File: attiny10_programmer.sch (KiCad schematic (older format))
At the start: 12 parts, among them J1 Conn_01x03, J2 AVR-ISP-6, Q1 Q_PNP_EBC, U1 SFH617A-1, U2 ATtiny10-TS

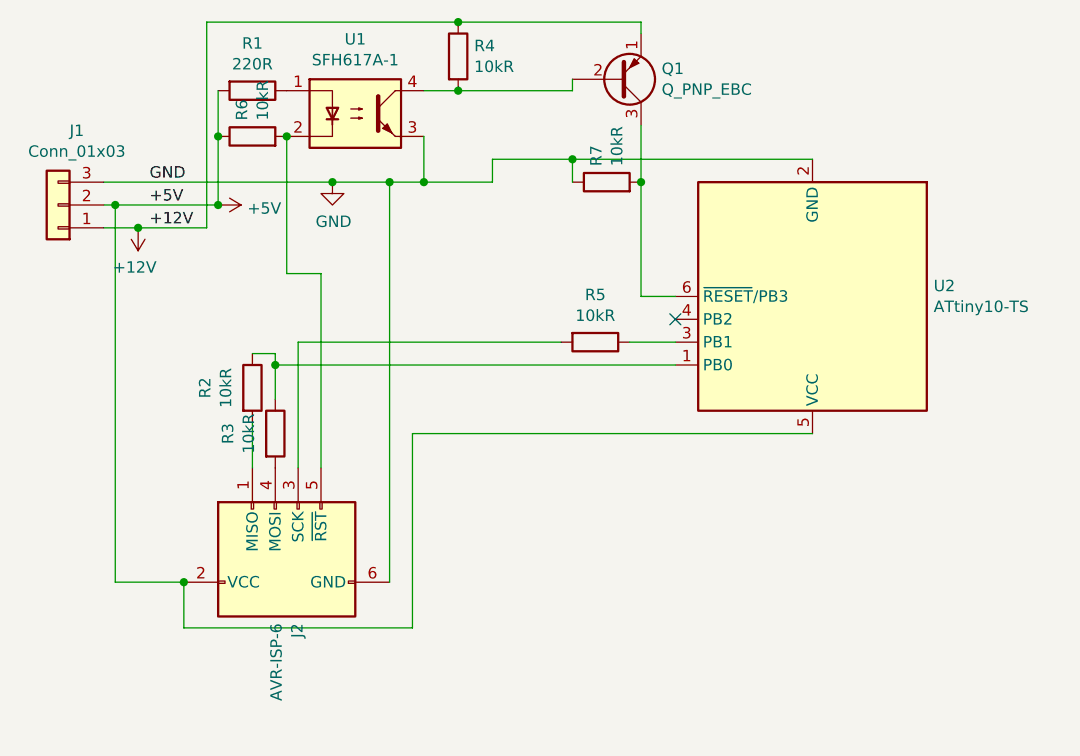
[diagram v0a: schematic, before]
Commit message: Add current limiting resistor on +12v
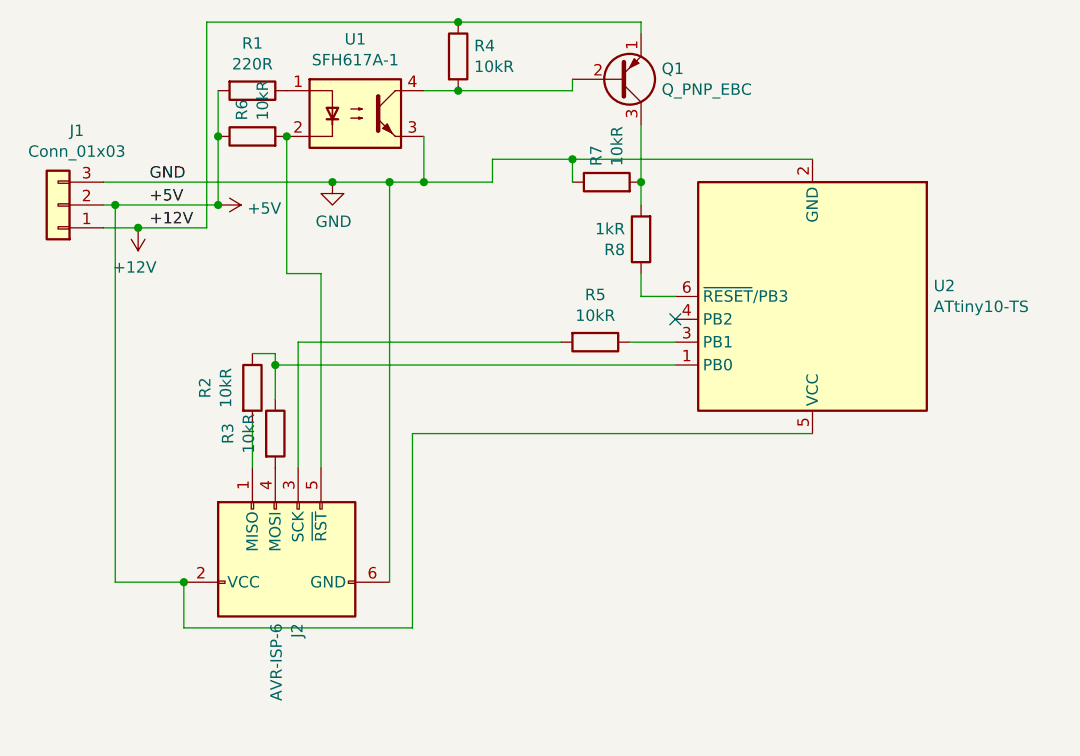
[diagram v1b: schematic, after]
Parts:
- added R8: 1kR, Resistor_SMD:R_0805_2012Metric, symbol Device:R
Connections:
- net at Q1.3 (C), R7.2: now also R8.2; no longer U2.6 (~RESET~/PB3)
- new net: R8.1, U2.6 (~RESET~/PB3)
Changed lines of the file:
@@
 Wire Wire Line
 	7100 3700 7100 3950
+$Comp
+L Device:R R8
+U 1 1 5DD237BE
+P 7100 4200
+F 0 "R8" H 7170 4246 50  0000 L CNN
+F 1 "1kR" H 7170 4155 50  0000 L CNN
+F 2 "Resistor_SMD:R_0805_2012Metric" V 7030 4200 50  0001 C CNN
+F 3 "~" H 7100 4200 50  0001 C CNN
+	1    7100 4200
+	-1   0    0    1
+$EndComp
 Wire Wire Line
-	7100 3950 7100 4450
+	7100 4050 7100 3950
 Connection ~ 7100 3950
+Wire Wire Line
+	7100 4350 7100 4450
 $EndSCHEMATC

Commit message: Fix&Update gitignore
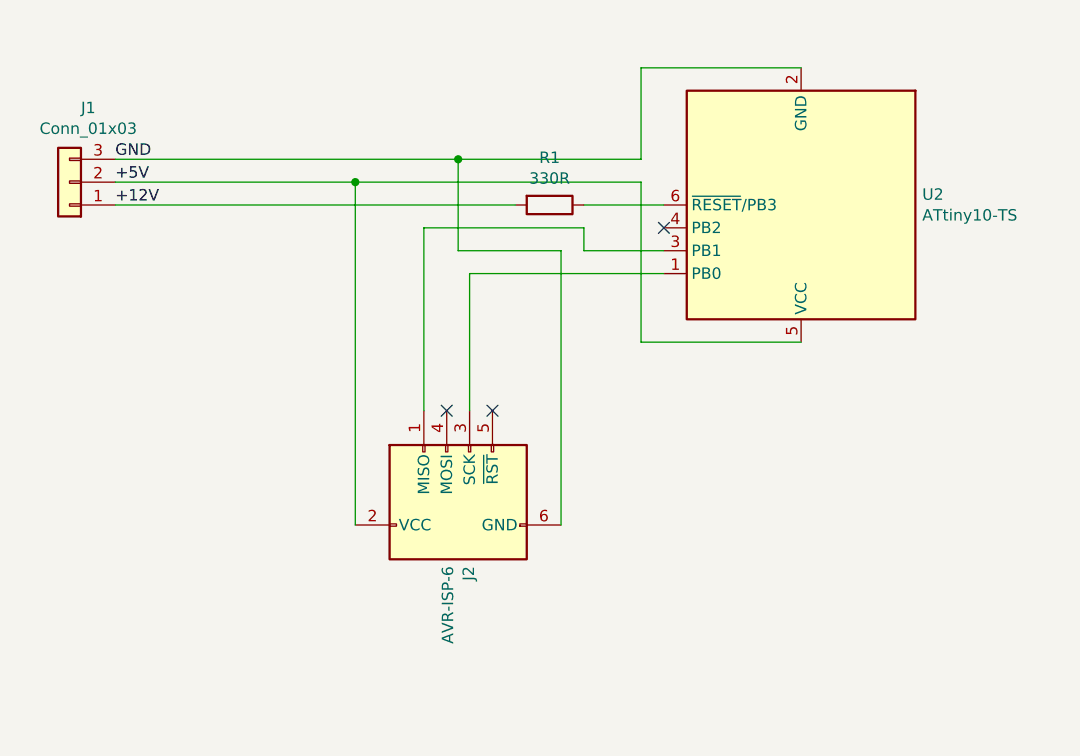
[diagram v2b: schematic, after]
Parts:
- removed Q1: Q_PNP_EBC, Package_TO_SOT_THT:TO-92, symbol Device:Q_PNP_EBC
- removed R2, R3, R4, R5, R6, R7: 10kR, Resistor_SMD:R_0805_2012Metric, symbol Device:R
- removed R8: 1kR, Resistor_SMD:R_0805_2012Metric, symbol Device:R
- removed U1: SFH617A-1, Package_DIP:DIP-4_W7.62mm, symbol Isolator:SFH617A-1
- R1: value 220R -> 330R
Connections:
- net +12V: now also R1.2
- net +5V: no longer R1.2
- net at R1.1: now also U2.6 (~RESET~/PB3)
- net at J2.1 (MISO): now also U2.3 (PB1)
- net at J2.3 (SCK): now also U2.1 (PB0)
- no-connect marks 1 -> 3
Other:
- moved on the sheet: J1, J2, U2
